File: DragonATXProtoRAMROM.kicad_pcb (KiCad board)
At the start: 2 copper layers, 151.2 x 56.7 mm, 29 parts, among them IC1 28C256, IC10 74LS244, IC11 74LS08, IC2 MK4164N, IC3 MK4164N, IC4 MK4164N, IC5 MK4164N, IC6 MK4164N, IC7 MK4164N, IC8 MK4164N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

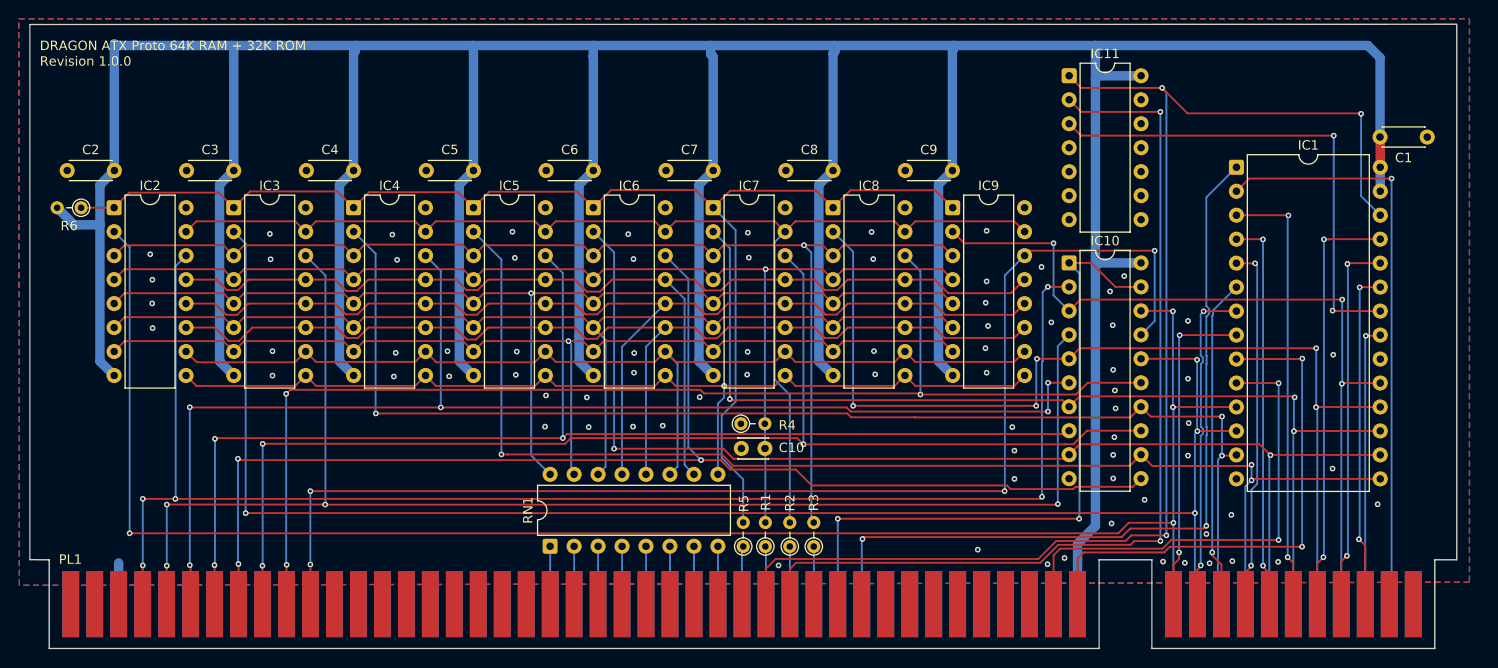
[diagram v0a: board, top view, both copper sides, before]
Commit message: update card edge spec
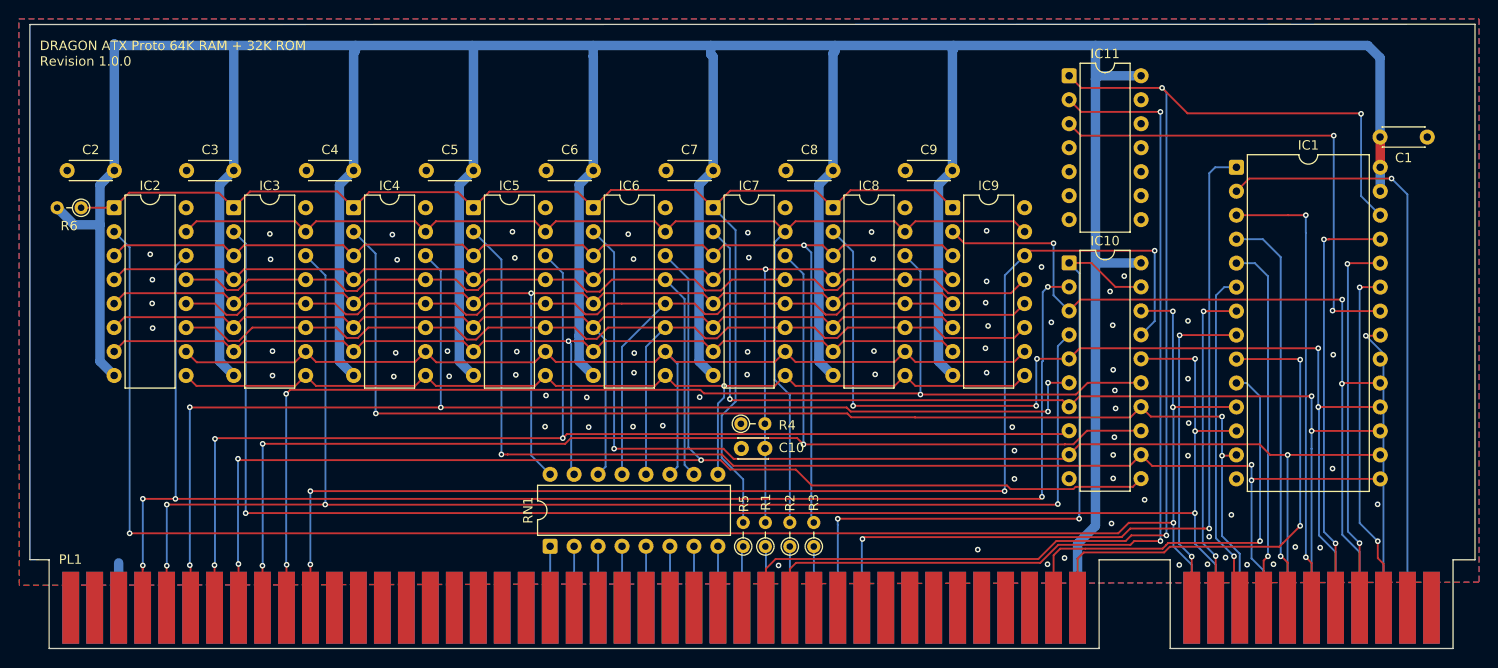
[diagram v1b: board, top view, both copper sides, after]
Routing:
- net /A0: track 51.2 -> 46.5 mm, vias 2 -> 1
- net /A1: track 56.5 -> 54.6 mm
- net /A7: track 47.4 -> 49.2 mm
- net /ROM_SEL: track 84.0 -> 85.3 mm
- net /A4: track 35.4 -> 36.7 mm
- net /D0: track 185.3 -> 186.4 mm
- net /A6: track 42.1 -> 43.0 mm, vias 2 -> 1
- net /D1: track 167.6 -> 168.3 mm
- net /D7: track 85.3 -> 86.0 mm
- net /A10: track 30.4 -> 31.1 mm
- net /A11: track 36.4 -> 37.2 mm
- net /D6: track 108.3 -> 109.0 mm
- net /A12: track 62.6 -> 63.2 mm
- net /A5: track 39.1 -> 39.3 mm, vias 2 -> 1
- net GND: vias 77 -> 79
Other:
- board size 151.2 x 56.7 mm -> 153.1 x 56.7 mm

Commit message: fix missing gnd pin connection
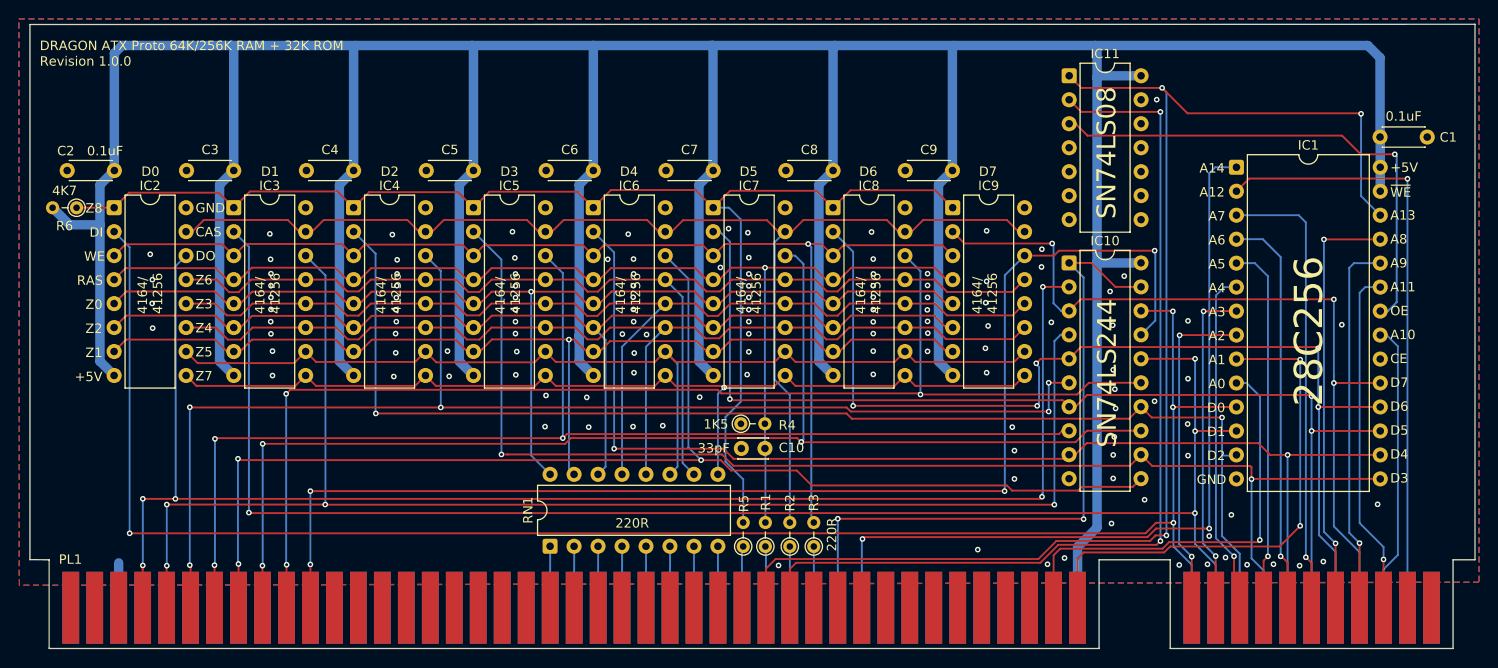
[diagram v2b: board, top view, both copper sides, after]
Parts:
- moved R6 0.48 mm to (76.1, 70.1)
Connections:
- IC11 pad 7: unconnected-(IC11E-GND-Pad7) -> GND
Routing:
- net /Z8: track 138.4 -> 140.4 mm
- net Net-(IC1-~{OE}): track 52.2 -> 53.7 mm, vias 2 -> 1
- net /Z0: track 115.3 -> 116.4 mm
- net /A12: track 63.2 -> 64.1 mm
- net /Z1: track 109.6 -> 110.6 mm
- net +5V: track 514.7 -> 513.7 mm
- net /RAS: track 122.1 -> 123.0 mm
- net /Z2: track 111.7 -> 112.6 mm
- net /CAS: track 127.2 -> 127.9 mm
- net /D7: track 86.0 -> 86.7 mm
- net /D.OUT: track 71.3 -> 72.0 mm
- net /Z3: track 115.6 -> 116.2 mm
- net /A9: track 40.5 -> 40.0 mm, vias 2 -> 1
- net /D5: track 110.6 -> 111.1 mm
- net /A7: track 49.2 -> 48.8 mm, vias 2 -> 1
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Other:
- board text added: "+5V"
- board text added: "28C256"
- board text added: "4164/ 41256"
- board text added: "A0"
- board text added: "A1"
- board text added: "A10"
- board text added: "A11"
- board text added: "A12"
- board text added: "A13"
- board text added: "A14"
- board text added: "A2"
- board text added: "A3"
- board text added: "A4"
- board text added: "A5"
- board text added: "A6"
- board text added: "A7"
- board text added: "A8"
- board text added: "A9"
- board text added: "CAS"
- board text added: "CE"
- board text added: "D0"
- board text added: "D1"
- board text added: "D2"
- board text added: "D3"
- board text added: "D4"
- board text added: "D5"
- board text added: "D6"
- board text added: "D7"
- board text added: "DI"
- board text added: "DO"
- board text added: "DRAGON ATX Proto 64K/256K RAM + 32K ROM"
- board text added: "GND"
- board text added: "OE"
- board text added: "RAS"
- board text added: "SN74LS08"
- board text added: "SN74LS244"
- board text added: "WE"
- board text added: "Z0"
- board text added: "Z1"
- board text added: "Z2"
- board text added: "Z3"
- board text added: "Z4"
- board text added: "Z5"
- board text added: "Z6"
- board text added: "Z7"
- board text added: "Z8"
- board text added: "~{WE}"
- board text removed: "DRAGON ATX Proto 64K RAM + 32K ROM"
